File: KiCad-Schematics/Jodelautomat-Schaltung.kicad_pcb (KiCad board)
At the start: 2 copper layers, 117.7 x 76.5 mm, 49 parts, among them J1 AudioJack3, J2 Conn_01x04_Pin, J3 Barrel_Jack, J4 Screw_Terminal_01x02, Q1 MMBT3904, Q10 MMBT3904, Q11 MMBT3904, Q12 MMBT3904, Q13 AO3400A, Q14 AO3400A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

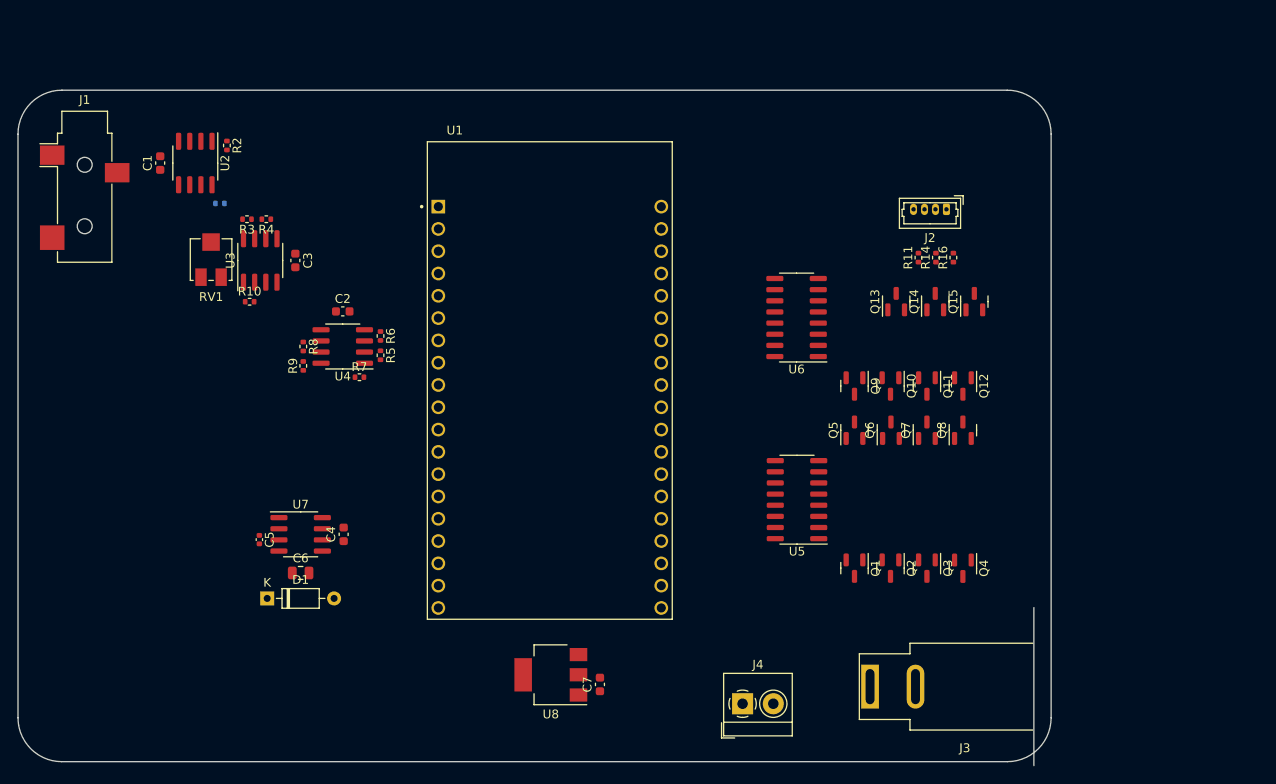
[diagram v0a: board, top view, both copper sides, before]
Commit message: added uart fft output
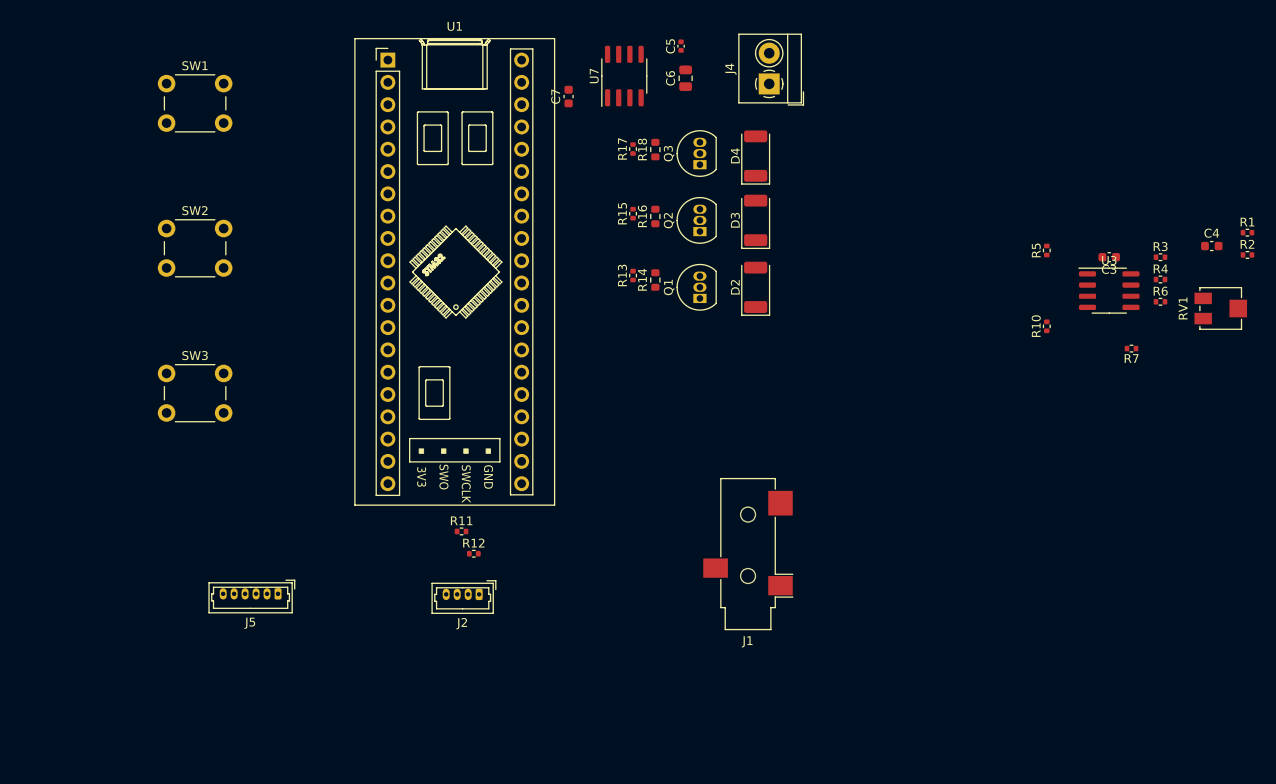
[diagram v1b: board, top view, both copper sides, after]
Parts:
- removed C1, C2: 100n, Capacitor_SMD:C_0603_1608Metric
- removed D1: 1N914, Diode_THT:D_DO-35_SOD27_P7.62mm_Horizontal
- removed J3: Barrel_Jack, Connector_BarrelJack:BarrelJack_SwitchcraftConxall_RAPC10U_Horizontal
- removed Q10, Q11, Q12, Q4, Q5, Q6, Q7, Q8, Q9: MMBT3904, Package_TO_SOT_SMD:SOT-23
- removed Q13, Q14, Q15: AO3400A, Package_TO_SOT_SMD:SOT-23
- removed R8, R9: 100k, Resistor_SMD:R_0402_1005Metric
- removed U2, U4: LM358, Package_SO:SOIC-8_3.9x4.9mm_P1.27mm
- removed U5, U6: 74HC595, Package_SO:SOIC-16_3.9x9.9mm_P1.27mm
- removed U8: AMS1117-5.0, Package_TO_SOT_SMD:SOT-223-3_TabPin2
- added D2: LED_R, LED_SMD:LED_2010_5025Metric, F.Cu at (132.4, 71.8)
- added D3: LED_G, LED_SMD:LED_2010_5025Metric, F.Cu at (132.4, 64.1)
- added D4: LED_B, LED_SMD:LED_2010_5025Metric, F.Cu at (132.4, 56.8)
- added J5: USART_Full_01x06, Connector_Molex:Molex_PicoBlade_53047-0610_1x06_P1.25mm_Vertical, F.Cu at (78.0, 106.7)
- added R12: 10k, Resistor_SMD:R_0402_1005Metric, F.Cu at (100.3, 102.1)
- added R13: 10k, Resistor_SMD:R_0402_1005Metric, F.Cu at (118.5, 70.4)
- added R15: 10k, Resistor_SMD:R_0402_1005Metric, F.Cu at (118.5, 63.4)
- added R17: 10k, Resistor_SMD:R_0402_1005Metric, F.Cu at (118.5, 56.0)
- added R18: 30R, Resistor_SMD:R_0603_1608Metric, F.Cu at (121.0, 56.1)
- added SW1: BTN_A, Button_Switch_THT:SW_PUSH_6mm, F.Cu at (65.3, 48.5)
- added SW2: BTN_B, Button_Switch_THT:SW_PUSH_6mm, F.Cu at (65.3, 65.1)
- added SW3: BTN_C, Button_Switch_THT:SW_PUSH_6mm, F.Cu at (65.3, 81.6)
- J2: value Conn_01x04_Pin -> I2C_5V_01x04
- Q1, Q2, Q3: value MMBT3904 -> BC337; footprint Package_TO_SOT_SMD:SOT-23 -> Package_TO_SOT_THT:TO-92_Inline
- R1: value 100k -> 50k; moved to F.Cu
- R11: value 100k -> 10k
- R14: value 100k -> 120R; footprint Resistor_SMD:R_0402_1005Metric -> Resistor_SMD:R_0603_1608Metric
- R16: value 100k -> 30R; footprint Resistor_SMD:R_0402_1005Metric -> Resistor_SMD:R_0603_1608Metric
- R2: value 100k -> 50k
- R3: value 10k -> 100k
- U1: value ESP32-DEVKITC-32D -> BlackPill_F401CCU6_SORTED; footprint ESP32-DEVKITC-32D:MODULE_ESP32-DEVKITC-32D -> STM32-Devboards:BlackPill_F401CCU6
- moved R1 117.1 mm to (188.5, 65.5)
- moved R2 116.9 mm to (188.5, 68.1), turned to 0 degrees
- moved RV1 115.2 mm to (185.4, 74.2), turned to 90 degrees
- moved C4 104.2 mm to (184.4, 67.1), turned to 0 degrees
- moved R3 104.2 mm to (178.6, 68.3), turned to 0 degrees
- moved R4 102.1 mm to (178.6, 70.9), turned to 0 degrees
- moved U3 96.8 mm to (172.7, 72.1), turned to 0 degrees
- moved C3 92.7 mm to (172.7, 68.3), turned to 180 degrees
- moved R10 90.9 mm to (165.6, 76.2), turned to 90 degrees
- moved R6 88.9 mm to (178.6, 73.4), turned to 0 degrees
- moved R7 88.0 mm to (175.3, 78.7), turned to 180 degrees
- moved J1 86.4 mm to (131.6, 102.1), turned to 180 degrees
- moved R5 76.8 mm to (165.6, 67.6), turned to 90 degrees
- moved C5 73.9 mm to (123.9, 44.3), turned to 90 degrees
- moved C6 71.4 mm to (124.5, 47.9), turned to 90 degrees
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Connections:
- net -12V renamed -5V
- C3 pad 2: +12V -> +5V
- C4 pad 2: +12V -> +5V
- C7 pad 1: GND -> +3.3V
- C7 pad 2: +5V -> GND
- J1 pad R: Net-(U2B-+) -> Net-(J1-PadR)
- J1 pad S: Net-(U2A-+) -> Net-(J1-PadS)
- J2 pad 3: Net-(J2-Pin_3) -> +5V
- J2 pad 4: +12V -> GND
- J4 pad 1: +12V -> +5V
- Q1 pad 2: LEDS_1_B -> Net-(Q1-B)
- Q1 pad 3: +3.3V -> Net-(Q1-E)
- Q2 pad 2: LEDS_1_B -> Net-(Q2-B)
- Q2 pad 3: PWM_OUT_1 -> Net-(Q2-E)
- Q3 pad 2: LEDS_1_B -> Net-(Q3-B)
- Q3 pad 3: PWM_OUT_2 -> Net-(Q3-E)
- R1 pad 1: Net-(U2B--) -> Net-(J1-PadS)
- R1 pad 2: Net-(U3B--) -> Net-(R1-Pad2)
- R10 pad 1: ADC_IN -> +3.3V
- R10 pad 2: Net-(U3A--) -> Net-(R10-Pad2)
- R11 pad 1: LEDS_1_B -> +5V
- R11 pad 2: GND -> Net-(J2-Pin_2)
- R14 pad 1: LEDS_1_G -> GND
- R14 pad 2: GND -> Net-(Q1-E)
- R16 pad 1: LEDS_1_R -> GND
- R16 pad 2: GND -> Net-(Q2-E)
- R2 pad 1: Net-(U2A--) -> Net-(J1-PadR)
- R2 pad 2: Net-(U3B--) -> Net-(R1-Pad2)
- R3 pad 2: Net-(R3-Pad2) -> Net-(U3A--)
- R5 pad 1: Net-(U4A-+) -> Net-(R10-Pad2)
- R5 pad 2: +3.3V -> GND
- R6 pad 1: GND -> Net-(U3A--)
- R6 pad 2: Net-(U4A-+) -> ADC_IN
- R7 pad 1: Net-(U4B--) -> Net-(R10-Pad2)
- R7 pad 2: Net-(U4A--) -> Net-(U3B--)
- RV1 pad 1: Net-(R3-Pad2) -> Net-(R1-Pad2)
- RV1 pad 2: GND -> unconnected-(RV1-Pad2)
- RV1 pad 3: Net-(U3A--) -> Net-(U3B--)
- U3 pad 4: +12V -> +5V
- U7 pad 8: +12V -> +5V
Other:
- board outline removed
